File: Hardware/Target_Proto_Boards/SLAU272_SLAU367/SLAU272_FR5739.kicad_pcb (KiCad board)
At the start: 2 copper layers, 70 x 40 mm, 38 parts, among them J1 USB_B_Micro, J10 GND, J11 +5V, J12 GND, J13 VSEL, J2 DEBUG, J3 PORT1, J4 LED_P4.1, J5 PORT2, J6 LogicAna, J7 JTAG/SBW, J8 PORT3, J9 VCC, SW1 TL-2203, SW2 RESET, U1 AMS1117-3.3, U2 MSP430FR5739IDAR, Y1 16M

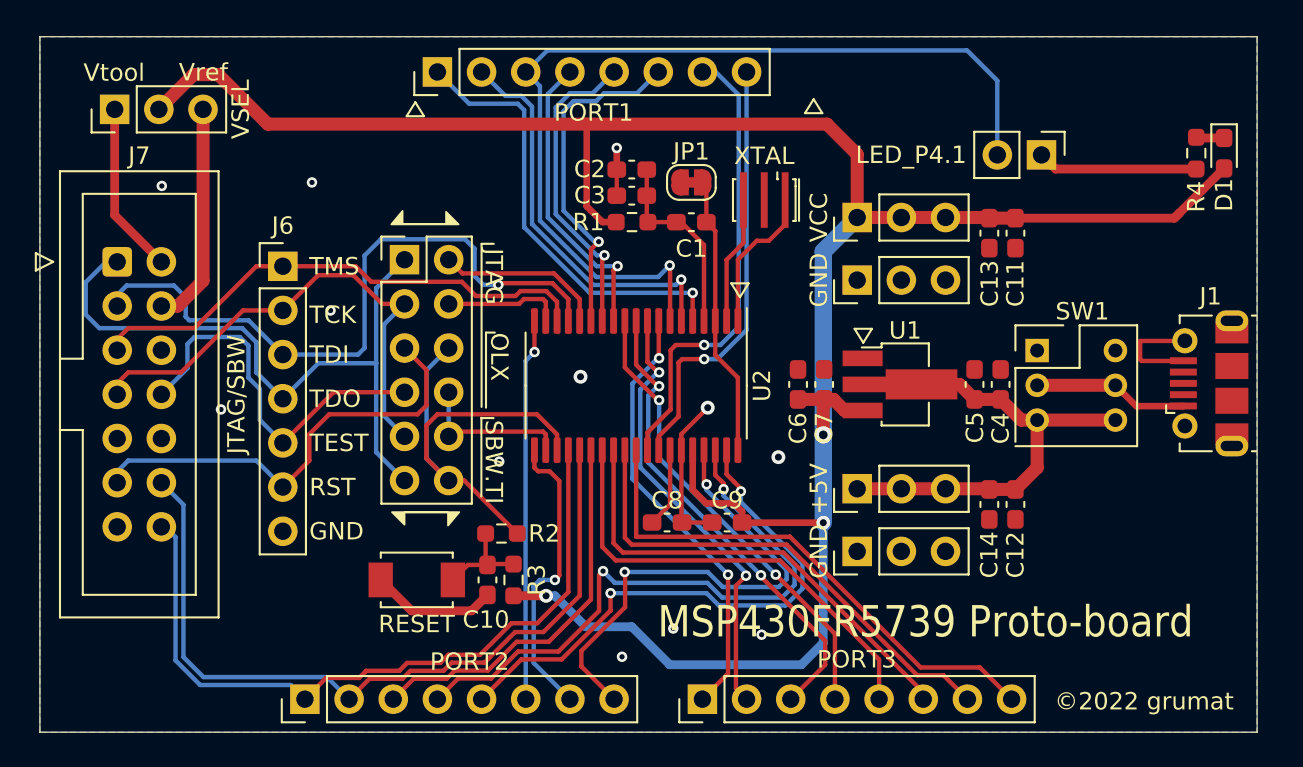
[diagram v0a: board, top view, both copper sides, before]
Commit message: Changed SLAU272_SLAU367 proto board to fully support FR5858 chips
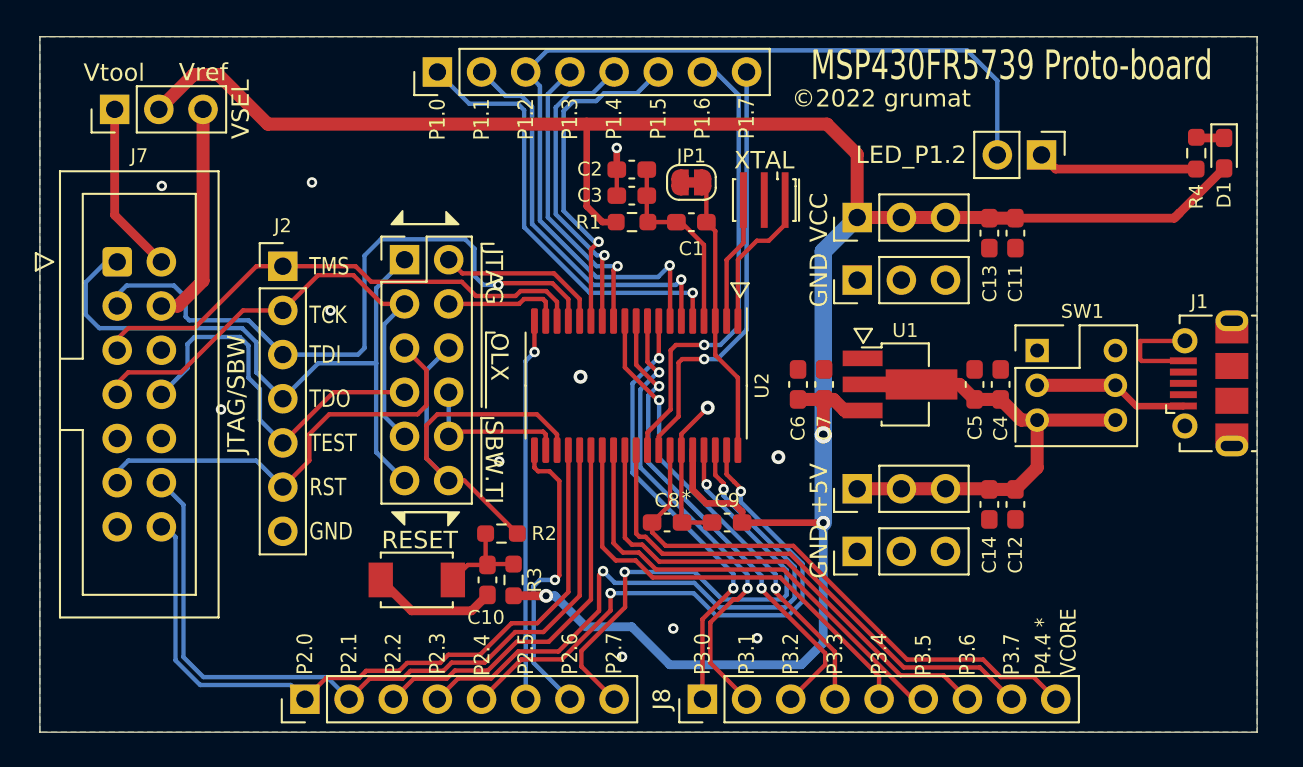
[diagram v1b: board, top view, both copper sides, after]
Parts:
- J5: renamed from J4; value LED_P4.1 -> LED_P1.2
- J8: footprint Connector_PinHeader_2.54mm:PinHeader_1x08_P2.54mm_Vertical -> Connector_PinHeader_2.54mm:PinHeader_1x09_P2.54mm_Vertical
- renumbered J6 to J2, J2 to J3, J3 to J4, J5 to J6
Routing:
- net /VCORE: track 4.59 -> 32.3 mm
- net /P3.1: track 25.6 -> 27.0 mm
- net /P2.7: track 28.4 -> 29.5 mm
- net /P2.3: track 35.4 -> 36.3 mm
- net /P2.4: track 32.0 -> 32.9 mm
- net /P3.4: track 26.5 -> 25.9 mm
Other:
- board text added: "*"
- board text added: "P1.0"
- board text added: "P1.1"
- board text added: "P1.2"
- board text added: "P1.3"
- board text added: "P1.4"
- board text added: "P1.5"
- board text added: "P1.6"
- board text added: "P1.7"
- board text added: "P2.0"
- board text added: "P2.1"
- board text added: "P2.2"
- board text added: "P2.3"
- board text added: "P2.4"
- board text added: "P2.5"
- board text added: "P2.6"
- board text added: "P2.7"
- board text added: "P3.0"
- board text added: "P3.1"
- board text added: "P3.2"
- board text added: "P3.3"
- board text added: "P3.4"
- board text added: "P3.5"
- board text added: "P3.6"
- board text added: "P3.7"
- board text added: "P4.4 * VCORE"

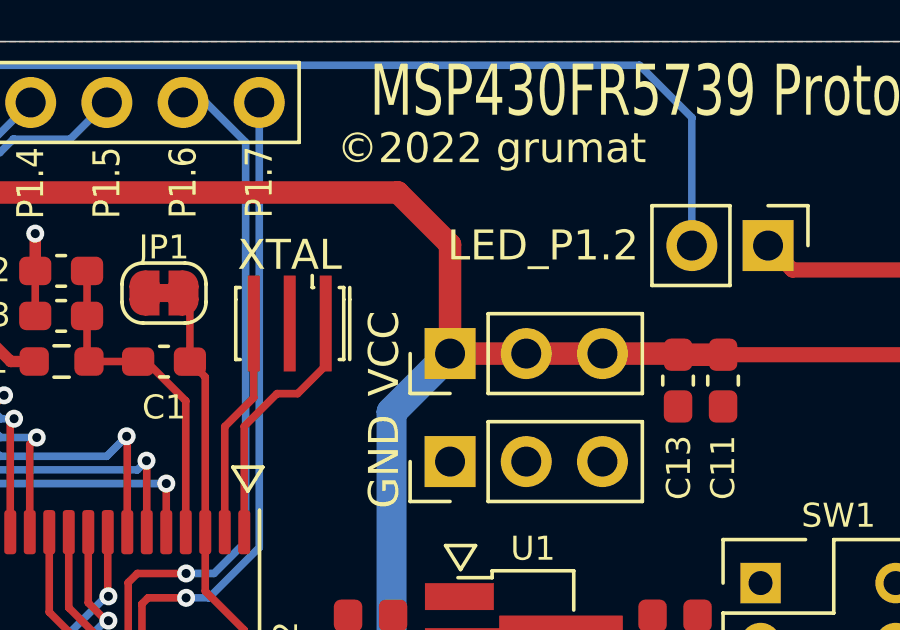
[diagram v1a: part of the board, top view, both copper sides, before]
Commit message: Added proto-board production files.
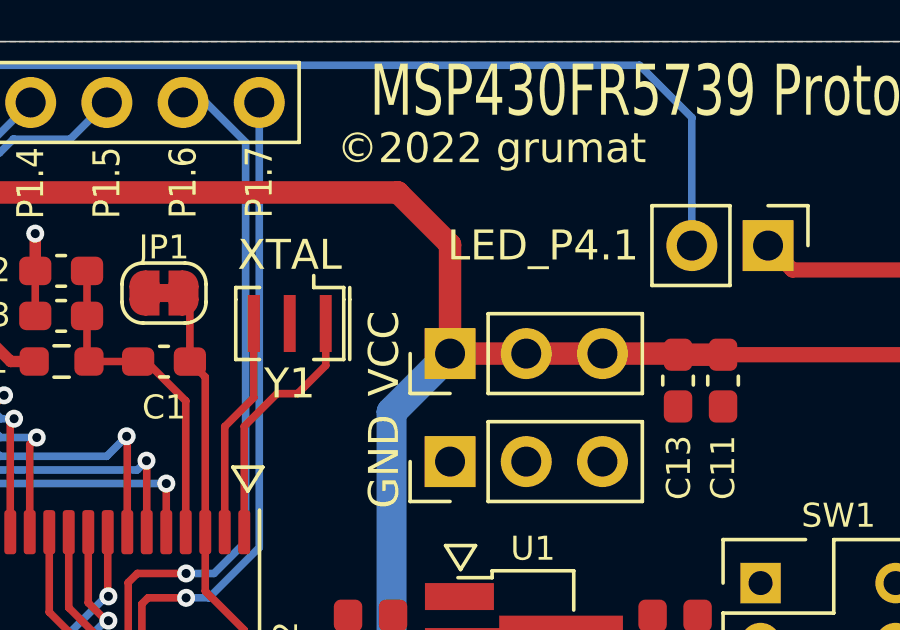
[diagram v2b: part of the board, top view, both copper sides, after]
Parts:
- J5: value LED_P1.2 -> LED_P4.1
- Y1: footprint Crystal:Resonator_SMD_Murata_CSTxExxV-3Pin_3.0x1.1mm_HandSoldering -> Crystal:Resonator_SMD_Murata_CSTxExxV-3Pin_3.0x1.1mm
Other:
- rule pad_to_mask_clearance: 0.1 -> 0
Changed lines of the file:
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@@
   )
   (setup
-    (pad_to_mask_clearance 0.1)
-    (solder_mask_min_width 0.2)
+    (stackup
+      (layer "F.SilkS" (type "Top Silk Screen"))
+      (layer "F.Paste" (type "Top Solder Paste"))
+      (layer "F.Mask" (type "Top Solder Mask") (thickness 0.01))
+      (layer "F.Cu" (type "copper") (thickness 0.035))
+      (layer "dielectric 1" (type "core") (thickness 1.51) (material "FR4") (epsilon_r 4.5) (loss_tangent 0.02))
+      (layer "B.Cu" (type "copper") (thickness 0.035))
+      (layer "B.Mask" (type "Bottom Solder Mask") (thickness 0.01))
+      (copper_finish "None")
+      (dielectric_constraints no)
+    )
+    (pad_to_mask_clearance 0)
     (aux_axis_origin 108 83)
     (grid_origin 108 83)
@@
       (psa4output false)
       (plotreference true)
-      (plotvalue true)
+      (plotvalue false)
       (plotinvisibletext false)
       (sketchpadsonfab false)
@@
     )
   )
-  (footprint "Crystal:Resonator_SMD_Murata_CSTxExxV-3Pin_3.0x1.1mm_HandSoldering" (layer "F.Cu")
+  (footprint "Crystal:Resonator_SMD_Murata_CSTxExxV-3Pin_3.0x1.1mm" (layer "F.Cu")
     (at 149.656 92.398 180)
     (descr "SMD Resomator/Filter Murata CSTCE, https://www.murata.com/en-eu/products/productdata/8801162264606/SPEC-CSTNE16M0VH3C000R0.pdf")
@@
     (property "Sheetname" "")
     (attr smd)
-    (fp_text reference "Y1" (at 0 -2.45) (layer "F.SilkS") hide
-      (effects (font (size 0.8 0.8) (thickness 0.15)))
-    )
-    (fp_text value "16M" (at 0 1.8) (layer "F.Fab")
+    (fp_text reference "Y1" (at 0 -2 180) (layer "F.SilkS")
+      (effects (font (size 1 1) (thickness 0.15)))
+    )
+    (fp_text value "16M" (at 0 1.8 180) (layer "F.Fab")
       (effects (font (size 0.2 0.2) (thickness 0.03)))
     )
-    (fp_text user "${REFERENCE}" (at 0.1 -0.05) (layer "F.Fab")
+    (fp_text user "${REFERENCE}" (at 0.1 -0.05 180) (layer "F.Fab")
       (effects (font (size 0.6 0.6) (thickness 0.08)))
     )
+    (fp_line (start 1.8 -1.2) (end 1.8 0.8) (layer "F.SilkS") (width 0.12))
+    (fp_line (start -1.8 0.8) (end -1.8 -1.2) (layer "F.SilkS") (width 0.12))
+    (fp_line (start 1.8 1.2) (end 1 1.2) (layer "F.SilkS") (width 0.12))
+    (fp_line (start 1 -1.2) (end 1.8 -1.2) (layer "F.SilkS") (width 0.12))
     (fp_line (start -1.8 0.8) (end -1.8 1.2) (layer "F.SilkS") (width 0.12))
+    (fp_line (start -0.8 1.2) (end -0.8 1.6) (layer "F.SilkS") (width 0.12))
+    (fp_line (start -1.8 -1.2) (end -0.8 -1.2) (layer "F.SilkS") (width 0.12))
+    (fp_line (start 1.8 0.8) (end 1.8 1.2) (layer "F.SilkS") (width 0.12))
+    (fp_line (start -2 0.8) (end -2 1.2) (layer "F.SilkS") (width 0.12))
     (fp_line (start -2 -1.2) (end -2 0.8) (layer "F.SilkS") (width 0.12))
-    (fp_line (start -0.75 1.2) (end -0.75 1.6) (layer "F.SilkS") (width 0.12))
-    (fp_line (start -1.8 0.8) (end -1.8 -1.2) (layer "F.SilkS") (width 0.12))
-    (fp_line (start -2 0.8) (end -2 1.2) (layer "F.SilkS") (width 0.12))
-    (fp_line (start -1.8 1.2) (end -1.65 1.2) (layer "F.SilkS") (width 0.12))
-    (fp_line (start 1.8 -1.2) (end 1.8 0.8) (layer "F.SilkS") (width 0.12))
-    (fp_line (start 1.8 1.2) (end 1.65 1.2) (layer "F.SilkS") (width 0.12))
-    (fp_line (start 1.8 -1.2) (end 1.65 -1.2) (layer "F.SilkS") (width 0.12))
-    (fp_line (start -0.75 1.2) (end -0.8 1.2) (layer "F.SilkS") (width 0.12))
-    (fp_line (start -1.8 -1.2) (end -1.65 -1.2) (layer "F.SilkS") (width 0.12))
-    (fp_line (start 1.8 0.8) (end 1.8 1.2) (layer "F.SilkS") (width 0.12))
-    (fp_line (start 1.75 -1.85) (end 1.75 1.85) (layer "F.CrtYd") (width 0.05))
-    (fp_line (start -1.75 1.85) (end -1.75 -1.85) (layer "F.CrtYd") (width 0.05))
-    (fp_line (start -1.75 -1.85) (end 1.75 -1.85) (layer "F.CrtYd") (width 0.05))
-    (fp_line (start 1.75 1.85) (end -1.75 1.85) (layer "F.CrtYd") (width 0.05))
+    (fp_line (start -0.8 1.2) (end -1.8 1.2) (layer "F.SilkS") (width 0.12))
+    (fp_line (start 1.75 1.2) (end -1.75 1.2) (layer "F.CrtYd") (width 0.05))
+    (fp_line (start -1.75 -1.2) (end 1.75 -1.2) (layer "F.CrtYd") (width 0.05))
+    (fp_line (start -1.75 1.2) (end -1.75 -1.2) (layer "F.CrtYd") (width 0.05))
+    (fp_line (start 1.75 -1.2) (end 1.75 1.2) (layer "F.CrtYd") (width 0.05))
+    (fp_line (start -1.5 0.3) (end -1.5 -0.8) (layer "F.Fab") (width 0.1))
     (fp_line (start 1.5 0.8) (end 1.5 -0.8) (layer "F.Fab") (width 0.1))
+    (fp_line (start -1 0.8) (end 1.5 0.8) (layer "F.Fab") (width 0.1))
+    (fp_line (start 1.5 -0.8) (end -1.5 -0.8) (layer "F.Fab") (width 0.1))
     (fp_line (start -1 0.8) (end -1.5 0.3) (layer "F.Fab") (width 0.1))
-    (fp_line (start -1 0.8) (end 1.5 0.8) (layer "F.Fab") (width 0.1))
-    (fp_line (start -1.5 0.3) (end -1.5 -0.8) (layer "F.Fab") (width 0.1))
-    (fp_line (start 1.5 -0.8) (end -1.5 -0.8) (layer "F.Fab") (width 0.1))
-    (pad "1" smd rect (at -1.2 0 180) (size 0.4 3.2) (layers "F.Cu" "F.Paste" "F.Mask")
+    (pad "1" smd rect (at -1.2 0 180) (size 0.4 1.9) (layers "F.Cu" "F.Paste" "F.Mask")
       (net 46 "/PJ.4") (pinfunction "1") (pintype "passive"))
-    (pad "2" smd rect (at 0 0 180) (size 0.4 3.2) (layers "F.Cu" "F.Paste" "F.Mask")
+    (pad "2" smd rect (at 0 0 180) (size 0.4 1.9) (layers "F.Cu" "F.Paste" "F.Mask")
       (net 1 "GND") (pinfunction "2") (pintype "passive"))
-    (pad "3" smd rect (at 1.2 0 180) (size 0.4 3.2) (layers "F.Cu" "F.Paste" "F.Mask")
+    (pad "3" smd rect (at 1.2 0 180) (size 0.4 1.9) (layers "F.Cu" "F.Paste" "F.Mask")
       (net 47 "/PJ.5") (pinfunction "3") (pintype "passive"))
     (model "${KICAD6_3DMODEL_DIR}/Crystal.3dshapes/Resonator_SMD_Murata_CSTxExxV-3Pin_3.0x1.1mm.wrl"
@@
       (effects (font (size 0.8 0.8) (thickness 0.15)))
     )
-    (fp_text value "LED_P1.2" (at 0 7.5 180) (layer "F.SilkS")
-      (effects (font (size 1 1) (thickness 0.15)))
-    )
+    (fp_text value "LED_P4.1" (at 0 7.5 180) (layer "F.SilkS")
+      (effects (font (size 1 1) (thickness 0.15)))
+    )

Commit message: Fixed regulator part#
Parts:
- U1: value AMS1117-3.3 -> HT7833
